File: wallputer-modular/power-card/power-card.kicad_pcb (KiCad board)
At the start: 2 copper layers, 99.7 x 99.7 mm, 134 parts, among them J2 Power, Q1 FQP27P06, Q2 IRLZ44N, SW1 reset, U1 TLC555CD, U12 74HC04, U16 74HC04, U17 74HC04, U18 74HC04, U2 74HC04, U3 74HC04

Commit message: begin wiring memory card
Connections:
- net NC30 renamed ROM_PGM/
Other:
- board text added: "ROM_PGM/"
- board text removed: "NC30"
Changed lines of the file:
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@@
 	(net 7 "VP{slash}")
 	(net 8 "SYNC")
-	(net 9 "NC30")
+	(net 9 "ROM_PGM{slash}")
 	(net 10 "D5")
 	(net 11 "A11")
@@
 			(layers "F.Cu" "F.Mask" "F.Paste")
 			(roundrect_rratio 0.25)
-			(net 9 "NC30")
+			(net 9 "ROM_PGM{slash}")
 			(pintype "input")
 		)
@@
 			(layers "*.Cu" "*.Mask")
 			(remove_unused_layers no)
-			(net 9 "NC30")
-			(pinfunction "NC")
+			(net 9 "ROM_PGM{slash}")
+			(pinfunction "ROM_PGM/")
 			(pintype "passive")
 		)
@@
 		)
 	)
-	(gr_text "NC30"
+	(gr_text "ROM_PGM/"
 		(at 97.79 102.235 0)
 		(layer "F.SilkS")

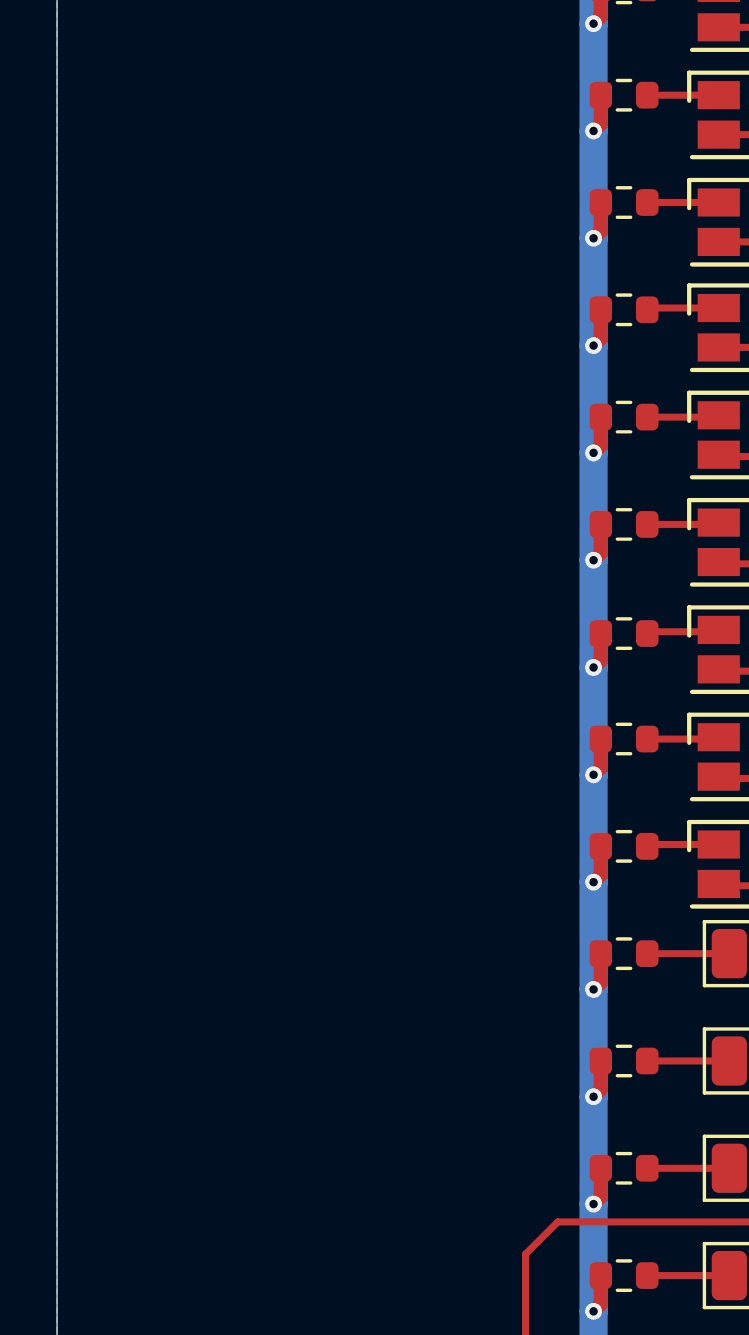
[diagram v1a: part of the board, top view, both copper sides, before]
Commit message: add card name
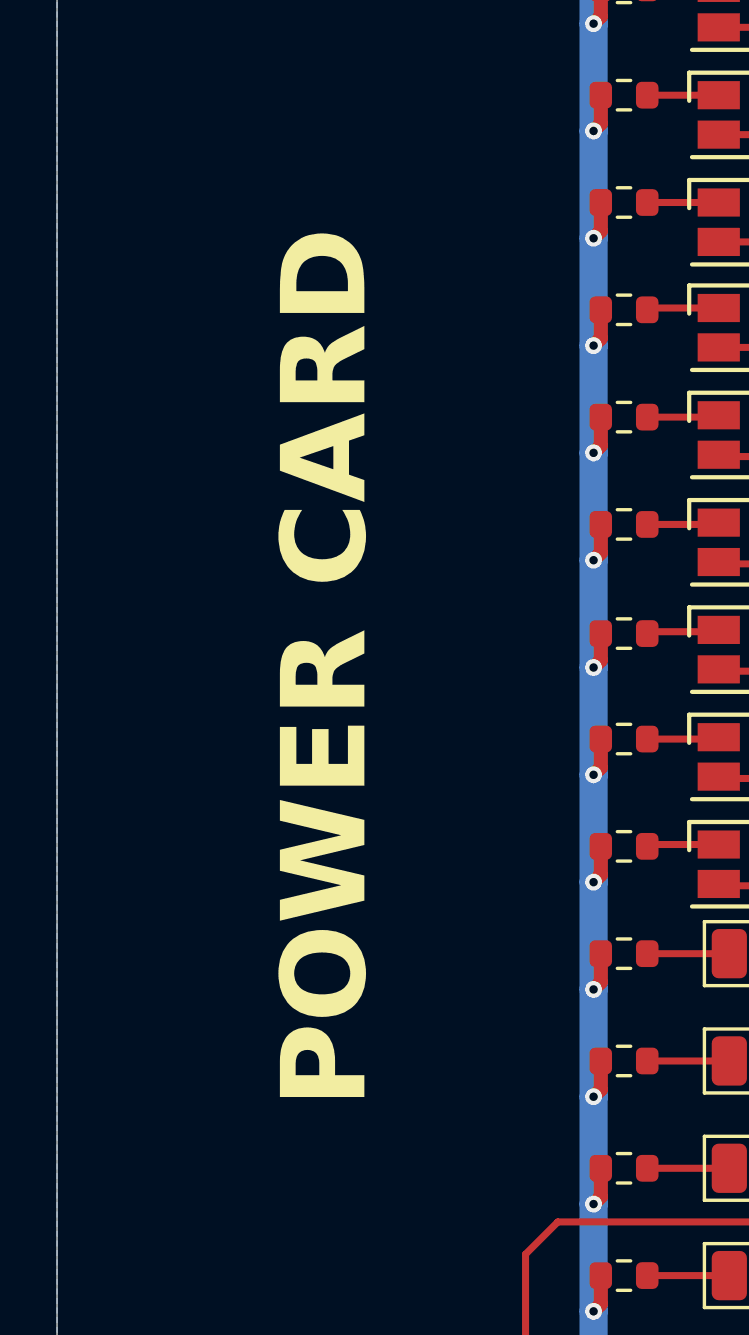
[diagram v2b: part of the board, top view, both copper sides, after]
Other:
- board text added: "POWER CARD"
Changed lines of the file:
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@@
+		)
+	)
+	(gr_text "POWER CARD\n"
+		(at 75.565 99.06 90)
+		(layer "F.SilkS")
+		(effects
+			(font
+				(size 3 3)
+				(thickness 0.5)
+				(bold yes)
+			)
 		)
 	)

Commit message: do cpu card layout; add git hook; fix project settings
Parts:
- removed R31: 10k, Resistor_THT:R_Axial_DIN0204_L3.6mm_D1.6mm_P2.54mm_Vertical
- moved C6 25.1 mm to (79.4, 115.2)
- moved SW1 25.1 mm to (69.0, 115.2)
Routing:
- net RES/: track 116.9 -> 96.1 mm
- net +5V: track 297.4 -> 287.5 mm
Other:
- board text added: "CARD"
- board text added: "POWER"
- board text added: "PROG"
- board text removed: "POWER CARD"
- board text removed: "ROM_PGM/"
